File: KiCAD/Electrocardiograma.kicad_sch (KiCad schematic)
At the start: 82 parts, among them J1 54-00174, J2 Conn_01x02_Pin, J3 USB_C_Receptacle_PowerOnly_6P, J4 Conn_01x02_Pin, J5 Conn_01x02_Pin, J6 Conn_01x04_Pin, U1 INA823DT, U2 ESP32-C3-WROOM-02, U3 TLV1117-33, U4 TLV4888, U5 TLV4888, U6 TLV1117-ADJ, U7 SC6038, U8 CH224K

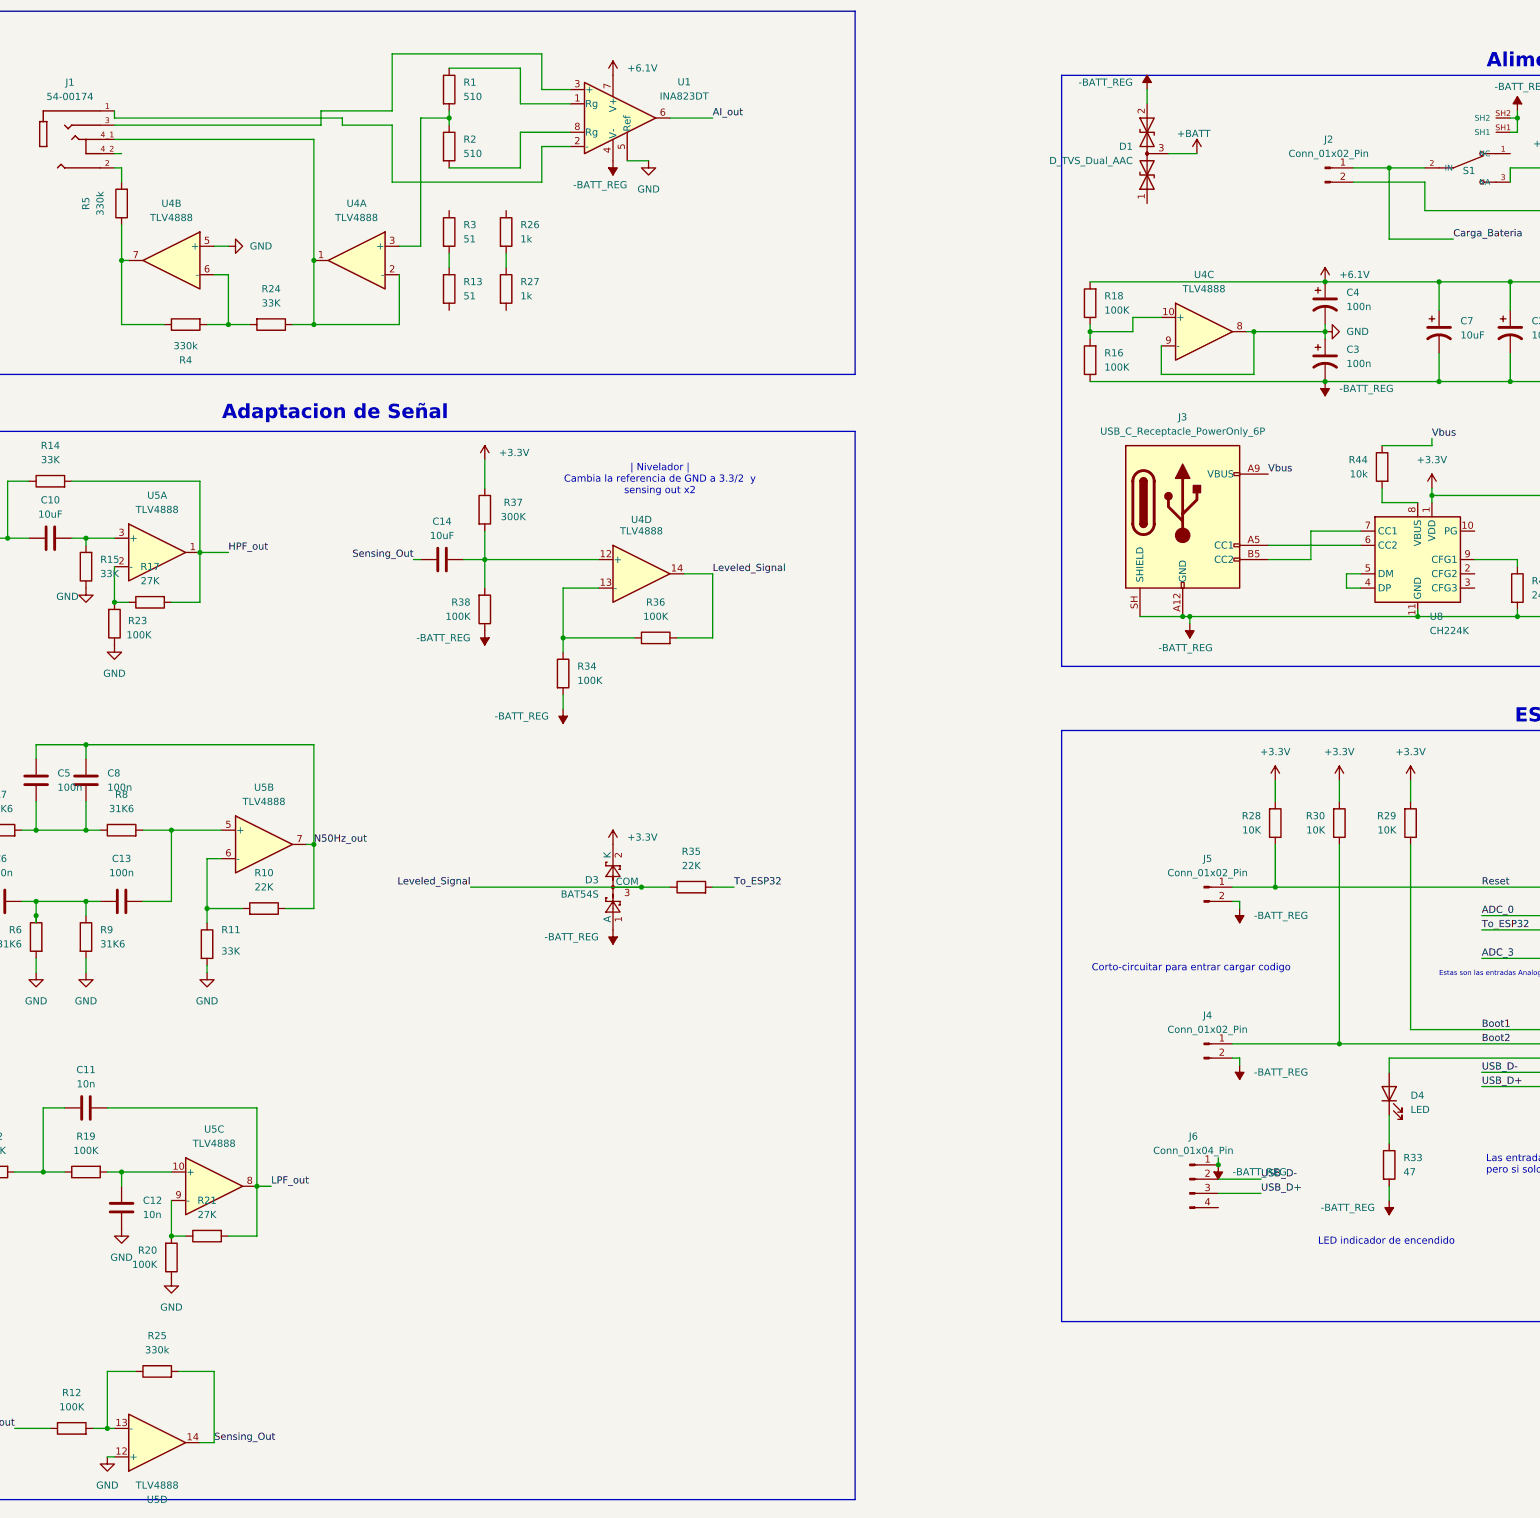
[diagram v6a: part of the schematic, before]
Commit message: PCB traces and schematics connections corrected and
Rerouted the jack 3.5 connections to be consistent with the signals from the male connector.
Changed the 100nF load capacitors for the GND opamp, for 10uF decoupling capacitors in the tension divider of the same opamp.
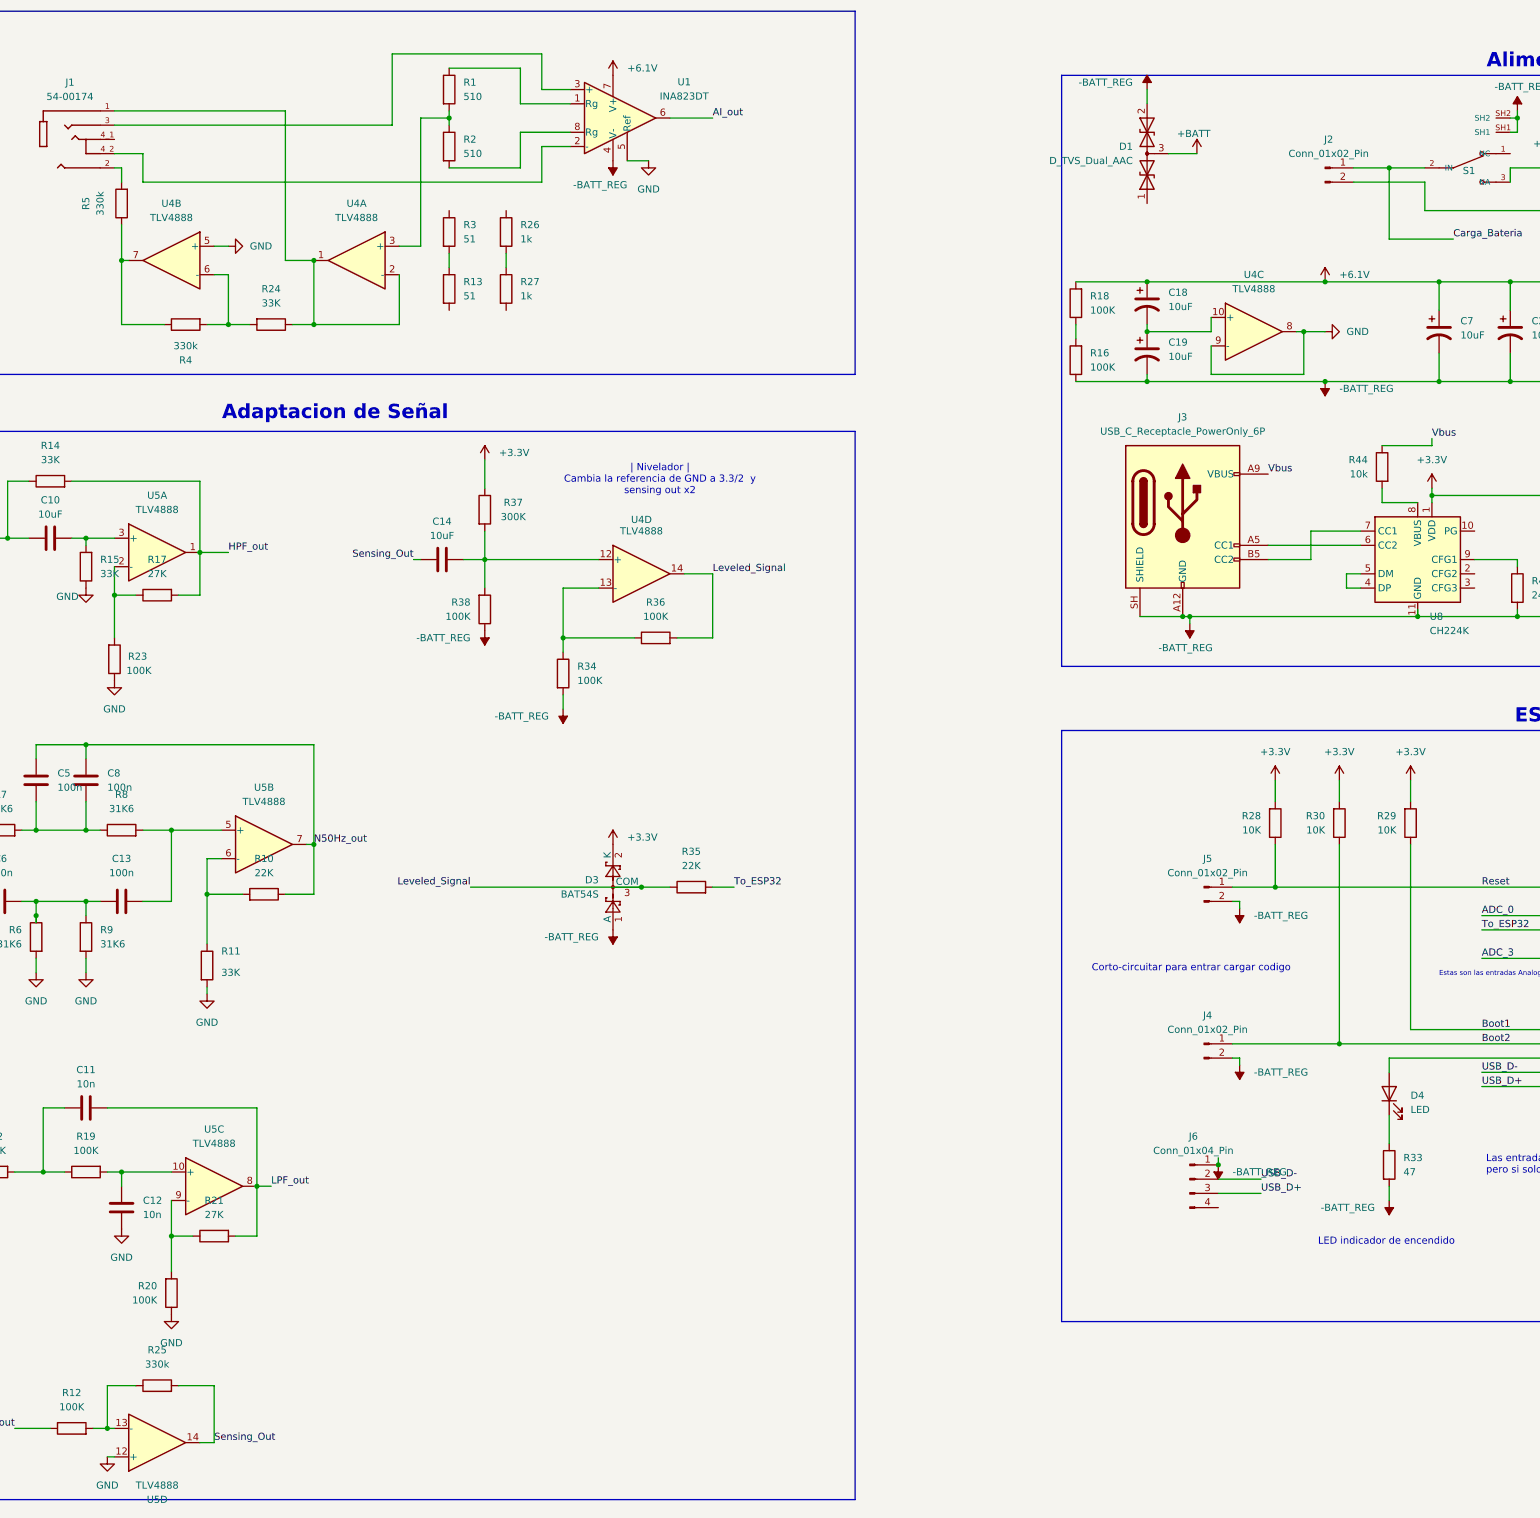
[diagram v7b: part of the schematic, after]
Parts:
- removed C3, C4: 100n, Capacitor_SMD:C_1206_3216Metric_Pad1.33x1.80mm_HandSolder, symbol Device:C_Polarized_US
- added C18, C19: 10uF, Capacitor_SMD:C_0805_2012Metric_Pad1.18x1.45mm_HandSolder, symbol Device:C_Polarized_US
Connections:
- net +6.1V: now also C18.1
- net -BATT_REG: now also C19.2
- net at R16.2, R18.1: no longer U4.10 (+)
- net at J1.1: now also R24.1, U4.1, U4.2 (-); no longer U1.2 (-)
- net at J1.4_2: now also U1.2 (-)
- new net: C18.2, C19.1, U4.10 (+)
- now unconnected: J1.4_1
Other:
- moved on the sheet: R10, R11, R16, R17, R18, R20, R21, R23, R25, U4C

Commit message: Nueva version de la placa, se hicieron pequeños cambios
Cambios en el Esquematico y PCB
se añadieron capacitores de 10nF, valor que está por calcularse
añadí espaciado de margen al USB-C
Meandros al cable de entrada al Amplificador Instrumental
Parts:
- added C20, C21, C22, C23, C24, C25, C26: 10nF, symbol Device:C
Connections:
- net -BATT_REG: now also C26.1
- net HPF_out: now also C20.2
- net LPF_out: now also C23.2
- net Leveled_Signal: now also C22.1
- net N50Hz_out: now also C21.2
- net Sensing_Out: now also C24.2
- net at C18.2, C19.1, U4.10 (+): now also R16.2, R18.1
- net at R12.2, R25.1, U5.13 (-): now also C24.1
- net at R10.1, R11.1, U5.6 (-): now also C21.1
- net at R26.2, R27.1: now also R1.2, R2.1, U4.3 (+)
- net at R27.2: now also R2.2, U1.8 (Rg)
- net at R17.1, R23.2, U5.2 (-): now also C20.1
- net at R13.1: no longer R3.2
- net at R20.2, R21.1, U5.9 (-): now also C23.1
- net at R31.2, R32.1, U6.1 (ADJ): now also C26.2
- net at R1.1, U1.1 (Rg): now also R26.1
- net at R34.1, R36.1, U4.13 (-): now also C22.2
- net at R24.2, R4.2, U4.6 (-): now also C25.2
- net at R4.1, R5.1, U4.7: now also C25.1
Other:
- note added: "Adquisicion de Señal Biofisiologica"
- note added: "Comentarios (Cuando se discutan se eliminan):"
- note added: "Hay que discutir sobre bajar el valor de resistencias de 100k y 26k7 del lazo de realimentación"
- note added: "NUEVO"
- note added: "Referencia de Vcc/2 Estabilizada con capacitores"
- note added: "Resistencias (120 Ohm) entre etapas que contengan capacitor INA --> HPF HPF --> BSF AMP_inv --> Nivelador"
- note added: "Resistencias de Rg de intercambio No se colocan, se deja el pad en el aire por si se necesita ajuste de ganancia"
- note added: "Se agregaron capacitores de 10nF a cada filtro El valor real del capacitor hay que calcularlo y aprobarlo en simulación"
- moved on the sheet: C1, C10, C11, C12, C13, C14, C15, C16, C17, C18, C19, C2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
